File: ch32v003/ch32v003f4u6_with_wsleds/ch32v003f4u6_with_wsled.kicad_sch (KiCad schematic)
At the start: 30 parts, among them J2 PGM, J4 USB_C_Receptacle_USB2.0, J5 HOLE, J6 HOLE, U1 CH32V003F4U6, U2 3.3vReg

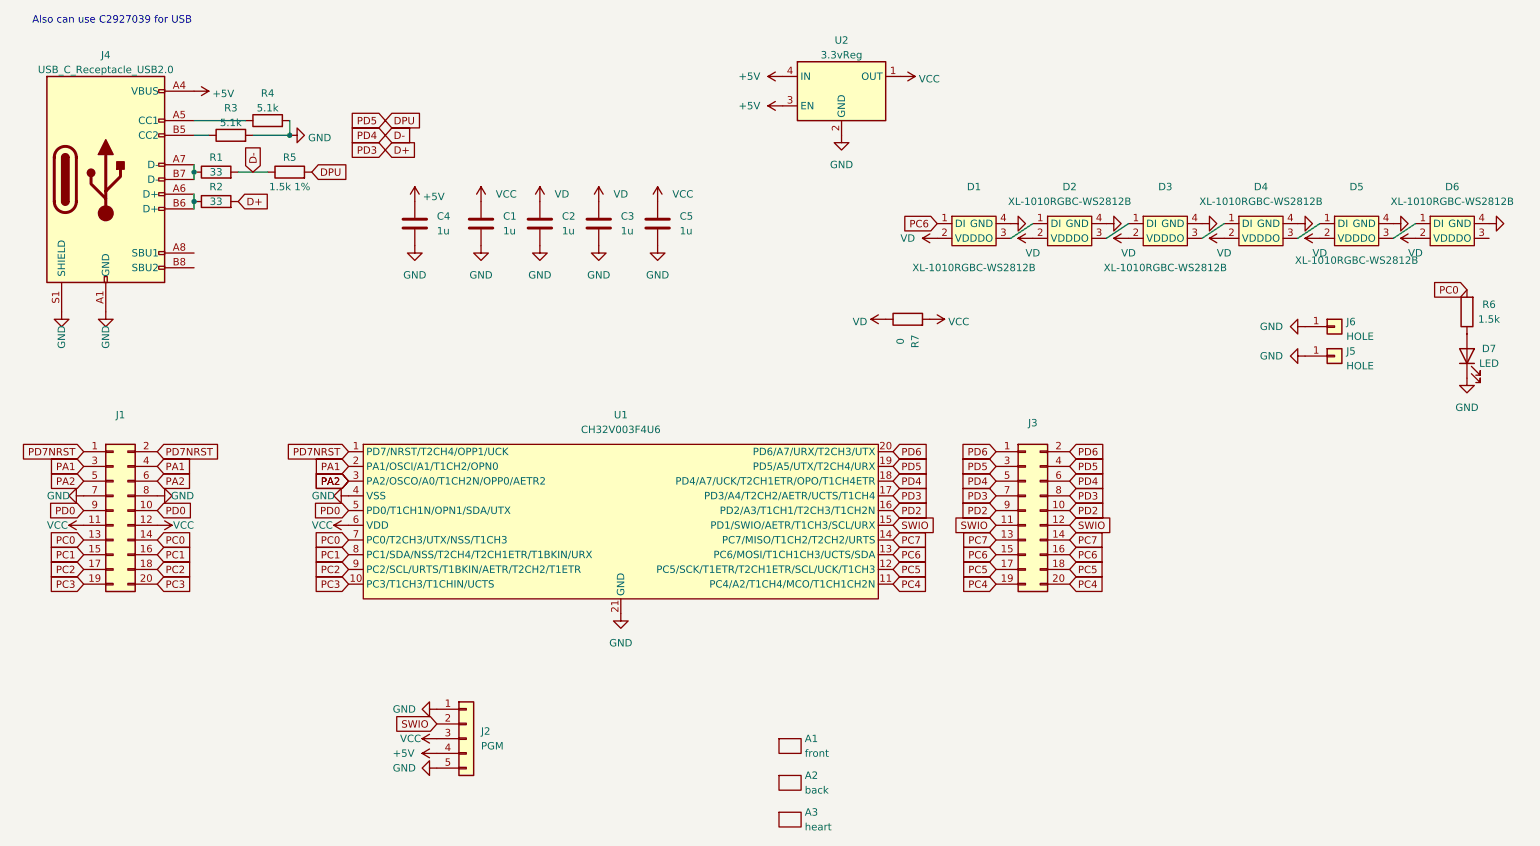
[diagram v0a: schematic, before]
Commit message: Replace some components with basic parts
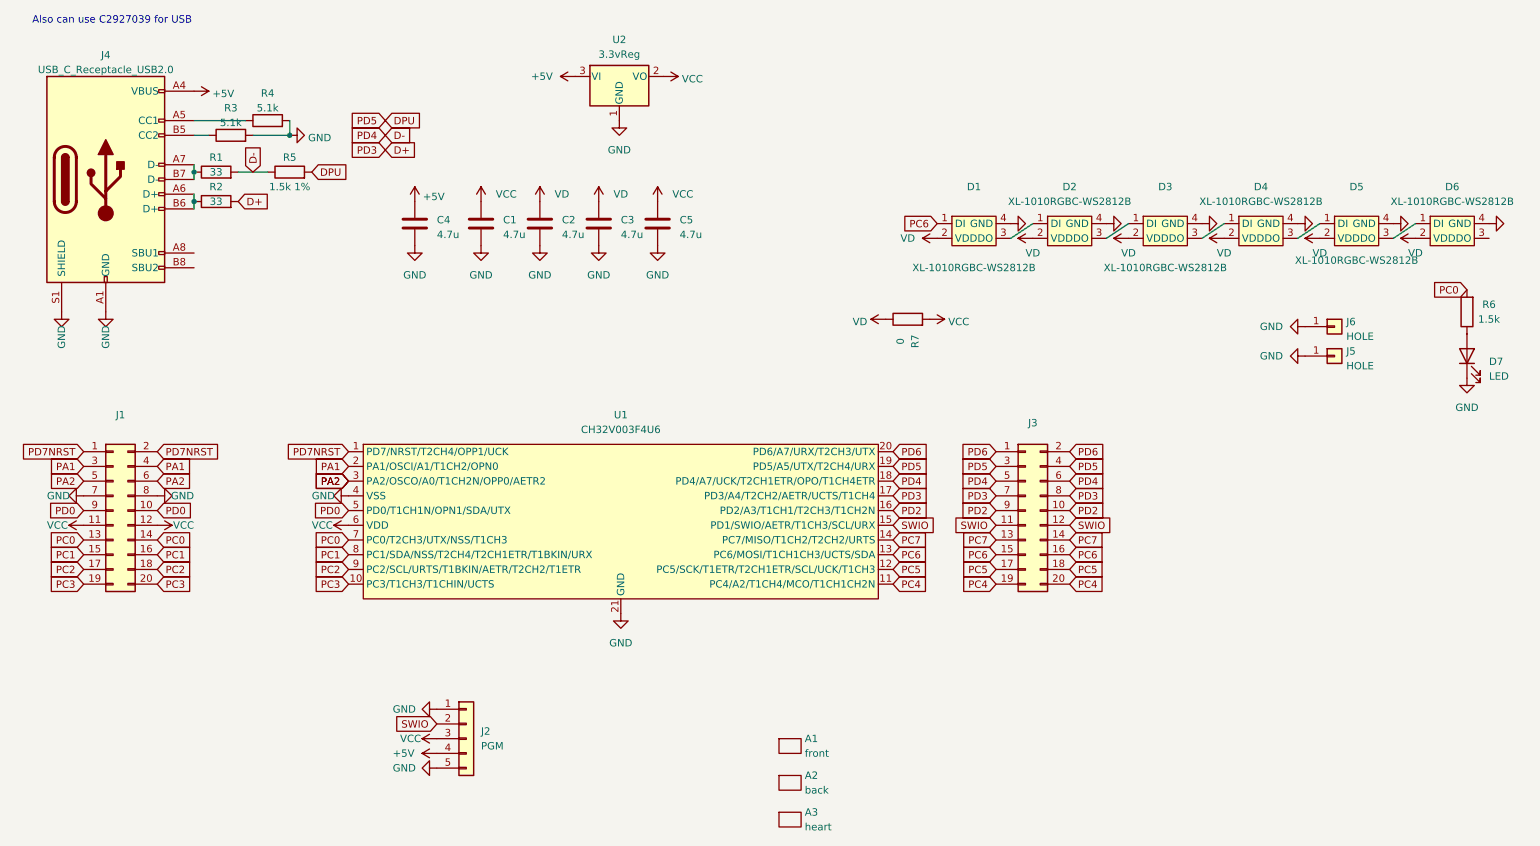
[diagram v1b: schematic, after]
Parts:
- removed U2: 3.3vReg, xdfn_reg:xdfn-reg, symbol Regulator_Linear:NCP115AMX120TCG
- added U2: 3.3vReg, Package_TO_SOT_SMD:SOT-23-3, symbol Regulator_Linear:XC6206PxxxMR
- C1, C2, C3, C4, C5: value 1u -> 4.7u; LCSC C237173 -> C23733
- D7: footprint LED_SMD:LED_0402_1005Metric -> LED_SMD:LED_0805_2012Metric; LCSC C74342 -> C34499
- R3, R4: LCSC C258132 -> C25905
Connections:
- net +5V: now also U2.3 (VI)
- net GND: now also U2.1 (GND)
- net VCC: now also U2.2 (VO)
